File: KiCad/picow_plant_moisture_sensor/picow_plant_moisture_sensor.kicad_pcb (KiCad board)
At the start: 4 copper layers, 74 x 52 mm, 52 parts, among them J2 AudioJack3, J3 Micro_SD_Card, J4 L77HDE15SD1CH4F, J7 Conn_02x03_Odd_Even, SW1 SW_Push, SW2 SW_Push, SW3 SW_Push, SW4 SW_Push, U1 TLV70033_SOT23-5, U2 PicoW, U3 NC7WZ16P6X

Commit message: First version done
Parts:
- removed C1, C2: 1u, Capacitor_SMD:C_0603_1608Metric
- removed C14, C15: 47u, Capacitor_SMD:C_0805_2012Metric
- removed C19: 10u, Capacitor_SMD:C_0603_1608Metric
- removed C4, C7, C8: 100n, Capacitor_SMD:C_0402_1005Metric
- removed R1, R2: 220, Resistor_SMD:R_0402_1005Metric
- removed R10, R11: 47, Resistor_SMD:R_0402_1005Metric
- removed R23, R24: 10k, Resistor_SMD:R_0402_1005Metric
- removed R26, R31, R36: 499, Resistor_SMD:R_0402_1005Metric
- removed R27, R32, R37: 1k, Resistor_SMD:R_0402_1005Metric
- removed R28, R33, R38: 2k, Resistor_SMD:R_0402_1005Metric
- removed R29, R34, R39: 4.02k, Resistor_SMD:R_0402_1005Metric
- removed R3, R4: 100, Resistor_SMD:R_0402_1005Metric
- removed R30, R35, R40: 8.06k, Resistor_SMD:R_0402_1005Metric
- removed R7, R8: 1.8K, Resistor_SMD:R_0402_1005Metric
- removed R9: DNF, Resistor_SMD:R_0402_1005Metric
- removed U1: TLV70033_SOT23-5, Package_TO_SOT_SMD:SOT-23-5
- removed U3: NC7WZ16P6X, Package_TO_SOT_SMD:SOT-363_SC-70-6
- added J1: Conn_01x03, Connector_PinHeader_2.54mm:PinHeader_1x03_P2.54mm_Horizontal, F.Cu at (106.4, 60.4)
- added J10: Conn_01x03, Connector_PinHeader_2.54mm:PinHeader_1x03_P2.54mm_Horizontal, F.Cu at (162.3, 65.5)
- added J11: Conn_01x03, Connector_PinHeader_2.54mm:PinHeader_1x03_P2.54mm_Horizontal, F.Cu at (162.3, 62.9)
- added J12: Conn_01x03, Connector_PinHeader_2.54mm:PinHeader_1x03_P2.54mm_Horizontal, F.Cu at (162.3, 60.4)
- added J13: Conn_01x03, Connector_PinHeader_2.54mm:PinHeader_1x03_P2.54mm_Horizontal, F.Cu at (162.3, 57.9)
- added J14: ADS1115, Connector_PinHeader_2.54mm:PinHeader_1x10_P2.54mm_Horizontal, F.Cu at (159.8, 57.9)
- added J15: ADS1115, Connector_PinHeader_2.54mm:PinHeader_1x10_P2.54mm_Horizontal, F.Cu at (103.9, 52.8)
- added J16: ADS1115, Connector_PinHeader_2.54mm:PinHeader_1x10_P2.54mm_Horizontal, F.Cu at (103.9, 78.2)
- added J5: Conn_01x03, Connector_PinHeader_2.54mm:PinHeader_1x03_P2.54mm_Horizontal, F.Cu at (106.4, 85.8)
- added J6: Conn_01x03, Connector_PinHeader_2.54mm:PinHeader_1x03_P2.54mm_Horizontal, F.Cu at (106.4, 83.3)
- added J8: Conn_01x03, Connector_PinHeader_2.54mm:PinHeader_1x03_P2.54mm_Horizontal, F.Cu at (106.4, 80.7)
- added J9: Conn_01x03, Connector_PinHeader_2.54mm:PinHeader_1x03_P2.54mm_Horizontal, F.Cu at (106.4, 78.2)
- J2: value AudioJack3 -> Conn_01x03; footprint RPi_Pico:CUI_SJ-3523-audio-jack -> Connector_PinHeader_2.54mm:PinHeader_1x03_P2.54mm_Horizontal
- J3: value Micro_SD_Card -> Conn_01x03; footprint Connector_Card:microSD_HC_Molex_104031-0811 -> Connector_PinHeader_2.54mm:PinHeader_1x03_P2.54mm_Horizontal
- J4: value L77HDE15SD1CH4F -> Conn_01x03; footprint RPi_Pico:DSUB-15-L77HDE15SD1CH4F -> Connector_PinHeader_2.54mm:PinHeader_1x03_P2.54mm_Horizontal
- moved J3 59.7 mm to (106.4, 55.3), turned to 90 degrees
- moved J2 55.1 mm to (106.4, 57.9), turned to 90 degrees
- moved J4 22.9 mm to (106.4, 52.8)
- moved SW4 22.4 mm to (111.0, 69.1)
- moved SW1 16.3 mm to (159.3, 89.4)
- moved SW2 16.0 mm to (111.0, 99.6)
- moved SW3 7.14 mm to (111.0, 92.0)
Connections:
- J2 pad 1: GND -> /AIN5
- J2 pad 2: /PWM_AUDIO_L -> +3V3
- J2 pad 3: /PWM_AUDIO_R -> GND
- J3 pad 1: /SD_DAT2 -> /AIN6
- J3 pad 2: /GPIO22 -> +3V3
- J3 pad 3: /GPIO18 -> GND
- J4 pad 1: /VGA_R -> /AIN7
- J4 pad 2: /VGA_G -> +3V3
- J4 pad 3: /VGA_B -> GND
- J7 pad 2: /SD_DAT2 -> /GPIO21
- J7 pad 4: /SD_DAT1 -> /GPIO20
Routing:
- net /HSYNC: track 89.2 -> 0.00 mm, vias 1 -> 0
- net /GPIO8: track 5.37 -> 91.0 mm
- net /GPIO9: track 5.37 -> 82.6 mm
- net /VSYNC: track 73.1 -> 0.00 mm, vias 1 -> 0
- net /GPIO5: track 56.4 -> 0.00 mm, vias 2 -> 0
- net +3V3: track 123.4 -> 173.4 mm, vias 4 -> 1
- net /GPIO18: track 35.4 -> 0.00 mm, vias 2 -> 0
- net /VGA_B: track 30.9 -> 0.00 mm, vias 1 -> 0
- net /GPIO19: track 29.9 -> 0.00 mm
- net /GPIO22: track 29.7 -> 0.00 mm, vias 2 -> 0
- net /VGA_G: track 28.5 -> 0.00 mm
- net /SD_DAT2: track 27.4 -> 0.00 mm
- net /VGA_R: track 25.9 -> 0.00 mm
- net GND: track 25.0 -> 0.00 mm, vias 60 -> 0
- net /SD_DAT1: track 20.3 -> 0.00 mm
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- removed copper zone on In1.Cu, net GND
- removed copper zone on In2.Cu, net GND
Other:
- board size 74 x 52 mm -> 78.7 x 55.9 mm
- copper layers 4 -> 2

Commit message: V1 done
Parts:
- J1, J10, J11, J12, J13, J2, J3, J4, J5, J6, J8, J9: footprint Connector_PinHeader_2.54mm:PinHeader_1x03_P2.54mm_Horizontal -> Connector_PinHeader_2.54mm:PinHeader_1x03_P2.54mm_Vertical
- J14, J15, J16: footprint Connector_PinHeader_2.54mm:PinHeader_1x10_P2.54mm_Horizontal -> Connector_PinHeader_2.54mm:PinHeader_1x10_P2.54mm_Vertical

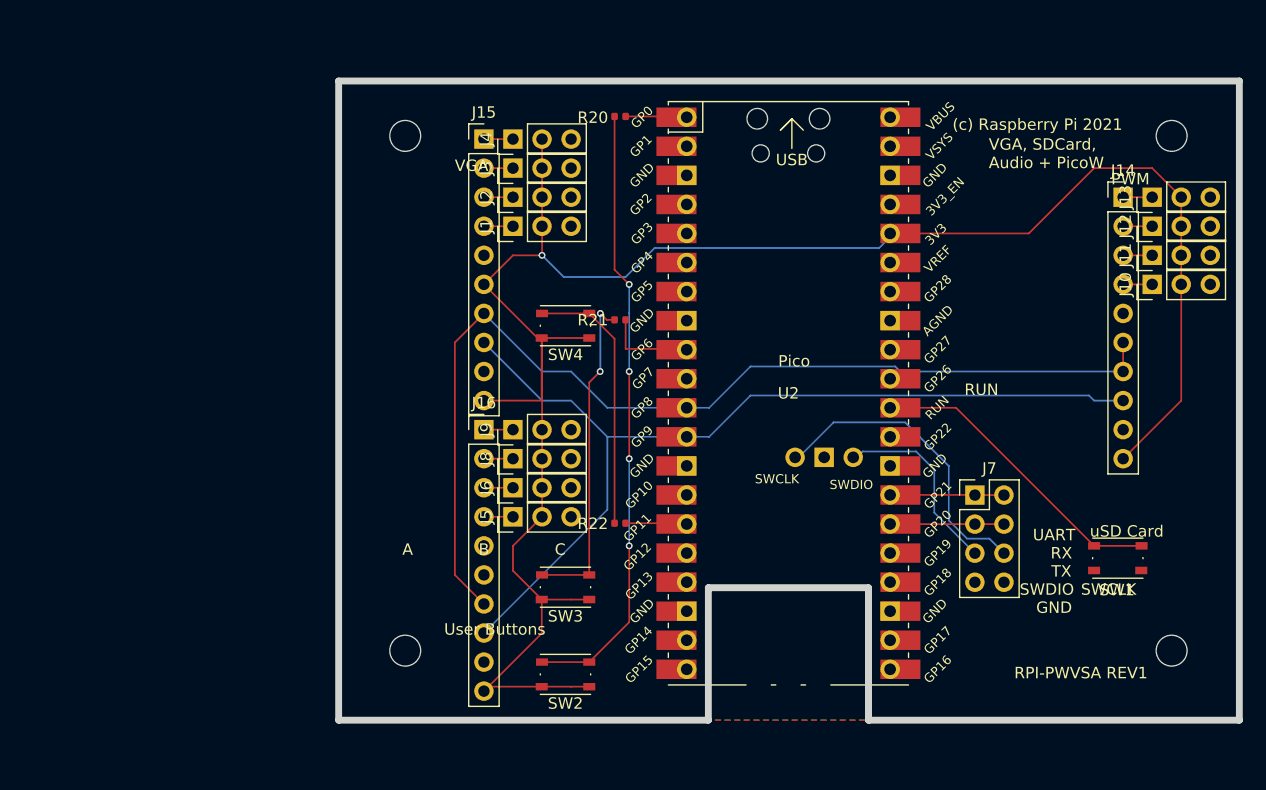
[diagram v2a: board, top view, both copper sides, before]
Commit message: 10 pcb design with ics instead of complete pcb on headers (#11)
* No traces

* Routing done

* Complete PCB design with component references

* Rev1 ordered
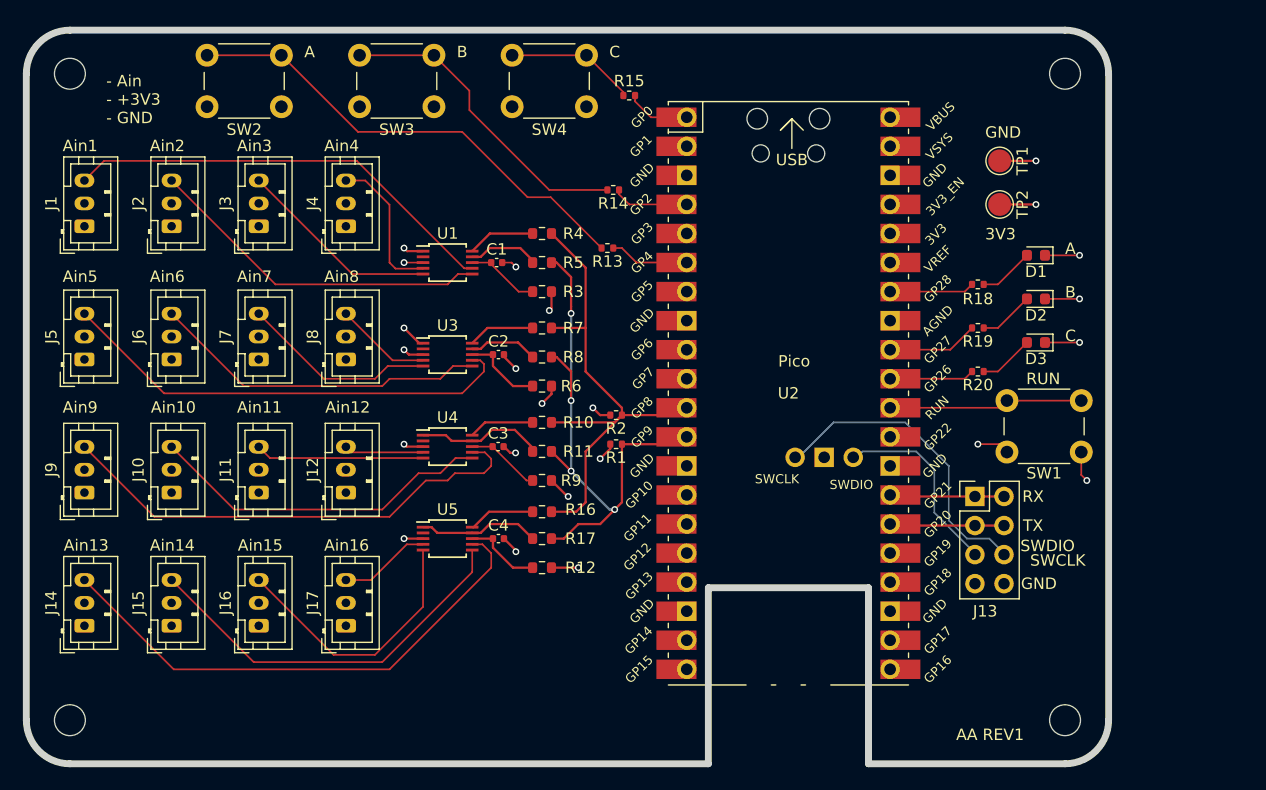
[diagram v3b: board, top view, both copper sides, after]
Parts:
- removed R21, R22: 1k, Resistor_SMD:R_0402_1005Metric
- added C1: 100n, Capacitor_SMD:C_0402_1005Metric, F.Cu at (105.0, 63.6)
- added C2: 100n, Capacitor_SMD:C_0402_1005Metric, F.Cu at (105.2, 71.6)
- added C3: 100n, Capacitor_SMD:C_0402_1005Metric, F.Cu at (105.1, 79.7)
- added C4: 100n, Capacitor_SMD:C_0402_1005Metric, F.Cu at (105.2, 87.7)
- added D1: LED, LED_SMD:LED_0603_1608Metric, F.Cu at (152.1, 62.9)
- added D2: LED, LED_SMD:LED_0603_1608Metric, F.Cu at (152.1, 66.8)
- added D3: LED, LED_SMD:LED_0603_1608Metric, F.Cu at (152.1, 70.6)
- added J17: Conn_01x03, Connector_JST:JST_PH_B3B-PH-K_1x03_P2.00mm_Vertical, F.Cu at (91.8, 95.3)
- added R1: 5k, Resistor_SMD:R_0402_1005Metric, F.Cu at (115.4, 79.5)
- added R10: 0, Resistor_SMD:R_0603_1608Metric, F.Cu at (109.0, 77.5)
- added R11: 0, Resistor_SMD:R_0603_1608Metric, F.Cu at (109.0, 80.1)
- added R12: 0, Resistor_SMD:R_0603_1608Metric, F.Cu at (109.0, 90.2)
- added R13: 1k, Resistor_SMD:R_0402_1005Metric, F.Cu at (114.7, 62.3)
- added R14: 1k, Resistor_SMD:R_0402_1005Metric, F.Cu at (115.2, 57.2)
- added R15: 1k, Resistor_SMD:R_0402_1005Metric, F.Cu at (116.6, 49.0)
- added R16: 0, Resistor_SMD:R_0603_1608Metric, F.Cu at (109.0, 85.4)
- added R17: 0, Resistor_SMD:R_0603_1608Metric, F.Cu at (109.0, 87.7)
- added R18: 330, Resistor_SMD:R_0402_1005Metric, F.Cu at (147.1, 65.5)
- added R19: 330, Resistor_SMD:R_0402_1005Metric, F.Cu at (147.1, 69.3)
- added R2: 5k, Resistor_SMD:R_0402_1005Metric, F.Cu at (115.4, 76.9)
- added R3: 0, Resistor_SMD:R_0603_1608Metric, F.Cu at (109.0, 66.1)
- added R4: 0, Resistor_SMD:R_0603_1608Metric, F.Cu at (109.0, 61.0)
- added R5: 0, Resistor_SMD:R_0603_1608Metric, F.Cu at (109.0, 63.6)
- added R6: 0, Resistor_SMD:R_0603_1608Metric, F.Cu at (109.0, 74.4)
- added R7: 0, Resistor_SMD:R_0603_1608Metric, F.Cu at (109.0, 69.3)
- added R8: 0, Resistor_SMD:R_0603_1608Metric, F.Cu at (109.0, 71.8)
- added R9: 0, Resistor_SMD:R_0603_1608Metric, F.Cu at (109.0, 82.6)
- added TP1: TestPoint, TestPoint:TestPoint_Pad_D2.0mm, F.Cu at (149.0, 54.7)
- added TP2: TestPoint, TestPoint:TestPoint_Pad_D2.0mm, F.Cu at (149.0, 58.5)
- added U1: ADS1115IDGS, Package_SO:TSSOP-10_3x3mm_P0.5mm, F.Cu at (100.7, 63.6)
- added U3: ADS1115IDGS, Package_SO:TSSOP-10_3x3mm_P0.5mm, F.Cu at (100.7, 71.6)
- added U4: ADS1115IDGS, Package_SO:TSSOP-10_3x3mm_P0.5mm, F.Cu at (100.7, 79.7)
- added U5: ADS1115IDGS, Package_SO:TSSOP-10_3x3mm_P0.5mm, F.Cu at (100.7, 87.7)
- J1, J10, J11, J12, J2, J3, J4, J5, J6, J8, J9: footprint Connector_PinHeader_2.54mm:PinHeader_1x03_P2.54mm_Vertical -> Connector_JST:JST_PH_B3B-PH-K_1x03_P2.00mm_Vertical
- J13: value Conn_01x03 -> Conn_02x03_Odd_Even; footprint Connector_PinHeader_2.54mm:PinHeader_1x03_P2.54mm_Vertical -> Connector_PinHeader_2.54mm:PinHeader_2x04_P2.54mm_Vertical
- J14, J15, J16: value ADS1115 -> Conn_01x03; footprint Connector_PinHeader_2.54mm:PinHeader_1x10_P2.54mm_Vertical -> Connector_JST:JST_PH_B3B-PH-K_1x03_P2.00mm_Vertical
- J7: value Conn_02x03_Odd_Even -> Conn_01x03; footprint Connector_PinHeader_2.54mm:PinHeader_2x04_P2.54mm_Vertical -> Connector_JST:JST_PH_B3B-PH-K_1x03_P2.00mm_Vertical
- R20: value 1k -> 330
- SW1, SW2, SW3, SW4: footprint Button_Switch_SMD:SW_Push_1P1T_NO_Vertical_Wuerth_434133025816 -> Button_Switch_THT:SW_PUSH_6mm
- moved J14 98.2 mm to (69.0, 95.3), turned to 90 degrees
- moved J10 87.6 mm to (76.6, 83.7)
- moved J11 80.8 mm to (84.2, 83.7)
- moved J12 74.2 mm to (91.8, 83.7)
- moved J7 63.7 mm to (84.2, 72.0), turned to 90 degrees
- moved SW2 55.5 mm to (86.2, 50.0)
- moved J15 50.6 mm to (76.6, 95.3), turned to 90 degrees
- moved SW3 43.6 mm to (99.5, 50.0)
- moved J5 39.9 mm to (69.0, 72.0)
- moved R20 38.4 mm to (147.1, 73.1)
- moved J9 37.9 mm to (69.0, 83.7)
- moved J1 37.5 mm to (69.0, 60.4)
- moved J6 31.9 mm to (76.6, 72.0)
- moved J13 30.4 mm to (146.8, 84.0), turned to 0 degrees
- moved J2 30.0 mm to (76.6, 60.4)
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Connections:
- J1 pad 1: /AIN4 -> GND
- J1 pad 3: GND -> /AIN0
- J10 pad 1: /AIN8 -> GND
- J10 pad 3: GND -> /AIN9
- J11 pad 1: /AIN9 -> GND
- J11 pad 3: GND -> /AIN10
- J12 pad 1: /AIN10 -> GND
- J12 pad 3: GND -> /AIN11
- J13 pad 1: /AIN11 -> /GPIO21
- J13 pad 2: +3V3 -> /GPIO21
- J13 pad 3: GND -> /GPIO20
- J14 pad 1: /AIN11 -> GND
- J14 pad 2: /AIN10 -> +3V3
- J14 pad 3: /AIN9 -> /AIN12
- J15 pad 1: /AIN7 -> GND
- J15 pad 2: /AIN6 -> +3V3
- J15 pad 3: /AIN5 -> /AIN13
- J16 pad 1: /AIN3 -> GND
- J16 pad 2: /AIN2 -> +3V3
- J16 pad 3: /AIN1 -> /AIN14
- J2 pad 1: /AIN5 -> GND
- J2 pad 3: GND -> /AIN1
- J3 pad 1: /AIN6 -> GND
- J3 pad 3: GND -> /AIN2
- J4 pad 1: /AIN7 -> GND
- J4 pad 3: GND -> /AIN3
- J5 pad 1: /AIN0 -> GND
- J5 pad 3: GND -> /AIN4
- J6 pad 1: /AIN1 -> GND
- J6 pad 3: GND -> /AIN5
- J7 pad 1: /GPIO21 -> GND
- J7 pad 2: /GPIO21 -> +3V3
- J7 pad 3: /GPIO20 -> /AIN6
- J8 pad 1: /AIN2 -> GND
- J8 pad 3: GND -> /AIN7
- J9 pad 1: /AIN3 -> GND
- J9 pad 3: GND -> /AIN8
- R20 pad 1: /GPIO0 -> Net-(D3-A)
- R20 pad 2: Net-(R20-Pad2) -> /GPIO26
- SW2 pad 2: Net-(R20-Pad2) -> Net-(R13-Pad2)
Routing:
- net +3V3: track 173.4 -> 16.8 mm, vias 1 -> 8
- net Net-(R20-Pad2): track 53.8 -> 0.00 mm, vias 4 -> 0
- net /AIN12: track 0.00 -> 45.7 mm
- net /GPIO8: track 91.0 -> 46.0 mm
- net Net-(R13-Pad2): track 0.00 -> 41.5 mm
- net /AIN8: track 2.54 -> 42.5 mm
- net /AIN4: track 2.54 -> 40.4 mm
- net /AIN0: track 2.54 -> 38.5 mm
- net /AIN13: track 0.00 -> 34.4 mm
- net /GPIO9: track 82.6 -> 50.1 mm, vias 0 -> 4
- net GND: track 0.00 -> 32.3 mm, vias 0 -> 15
- net /AIN9: track 2.54 -> 30.4 mm
- net /AIN1: track 2.54 -> 30.4 mm
- net /AIN5: track 2.54 -> 29.6 mm
- net /AIN14: track 0.00 -> 23.8 mm
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- added copper zone on In2.Cu, net +3V3
- added copper zone on In1.Cu, net GND
- removed copper zone on B.Cu, net GND
- removed copper zone on F.Cu, net GND
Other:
- board size 78.7 x 55.9 mm -> 94.6 x 64.1 mm
- copper layers 2 -> 4
- board text added: "- Ain - +3V3 - GND"
- board text added: "3V3"
- board text added: "AA REV1"
- board text added: "Ain1"
- board text added: "Ain10"
- board text added: "Ain11"
- board text added: "Ain12"
- board text added: "Ain13"
- board text added: "Ain14"
- board text added: "Ain15"
- board text added: "Ain16"
- board text added: "Ain2"
- board text added: "Ain3"
- board text added: "Ain4"
- board text added: "Ain5"
- board text added: "Ain6"
- board text added: "Ain7"
- board text added: "Ain8"
- board text added: "Ain9"
- board text removed: "(c) Raspberry Pi 2021"
- board text removed: "PWM"
- board text removed: "RPI-PWVSA REV1"
- board text removed: "UART"
- board text removed: "User Buttons"
- board text removed: "VGA"
- board text removed: "VGA, SDCard, Audio + PicoW"
- board text removed: "uSD Card"

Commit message: Add rev2 (#33)
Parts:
- added R21: 5k, Resistor_SMD:R_0603_1608Metric, F.Cu at (144.5, 78.8)
- added R22: 5k, Resistor_SMD:R_0603_1608Metric, F.Cu at (144.5, 81.3)
- added TP3: TestPoint, TestPoint:TestPoint_Pad_D2.0mm, F.Cu at (97.5, 56.0)
- added TP4: TestPoint, TestPoint:TestPoint_Pad_D2.0mm, F.Cu at (101.3, 57.2)
- added U6: 24LC16, 24LC16B-I_SN:SOIC127P600X175-8N, F.Cu at (149.7, 99.1)
- C1, C2, C3, C4: footprint Capacitor_SMD:C_0402_1005Metric -> Capacitor_SMD:C_0603_1608Metric
- R1, R13, R14, R15, R18, R19, R2, R20: footprint Resistor_SMD:R_0402_1005Metric -> Resistor_SMD:R_0603_1608Metric
- moved R14 1.14 mm to (114.0, 57.2)
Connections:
- J13 pad 1: /GPIO21 -> /GPIO17
- J13 pad 2: /GPIO21 -> /SWCLK
- J13 pad 3: /GPIO20 -> /GPIO16
- J13 pad 4: /GPIO20 -> GND
- J13 pad 5: /SWDIO -> GND
- J13 pad 6: /SWCLK -> /SWDIO
- R10 pad 2: /GPIO8 -> /GPIO9
- R11 pad 2: /GPIO9 -> /GPIO8
- R16 pad 2: /GPIO8 -> /GPIO9
- R17 pad 2: /GPIO9 -> /GPIO8
- R4 pad 2: /GPIO8 -> /GPIO9
- R5 pad 2: /GPIO9 -> /GPIO8
- R7 pad 2: /GPIO8 -> /GPIO9
- R8 pad 2: /GPIO9 -> /GPIO8
- U1 pad 4: /AIN3 -> /AIN0
- U1 pad 5: /AIN2 -> /AIN1
- U1 pad 6: /AIN1 -> /AIN2
- U1 pad 7: /AIN0 -> /AIN3
- U3 pad 4: /AIN7 -> /AIN4
- U3 pad 5: /AIN6 -> /AIN5
- U3 pad 6: /AIN5 -> /AIN6
- U3 pad 7: /AIN4 -> /AIN7
- U4 pad 4: /AIN11 -> /AIN8
- U4 pad 5: /AIN10 -> /AIN9
- U4 pad 6: /AIN9 -> /AIN10
- U4 pad 7: /AIN8 -> /AIN11
- U5 pad 4: /AIN15 -> /AIN12
- U5 pad 5: /AIN14 -> /AIN13
- U5 pad 6: /AIN13 -> /AIN14
- U5 pad 7: /AIN12 -> /AIN15
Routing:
- net /GPIO21: track 10.0 -> 41.9 mm
- net /GPIO20: track 10.0 -> 38.5 mm
- net /GPIO8: track 46.0 -> 64.6 mm, vias 0 -> 2
- net /GPIO17: track 0.00 -> 17.5 mm
- net /GPIO16: track 0.00 -> 16.5 mm
- net /AIN12: track 45.7 -> 30.9 mm
- net /AIN13: track 34.4 -> 23.1 mm
- net /AIN8: track 42.5 -> 33.3 mm
- net /AIN10: track 14.8 -> 22.8 mm
- net /AIN9: track 30.4 -> 24.2 mm
- net /GPIO9: track 50.1 -> 55.8 mm
- net +3V3: track 16.8 -> 22.4 mm, vias 8 -> 11
- net GND: track 32.3 -> 37.7 mm, vias 15 -> 17
- net /AIN4: track 40.4 -> 35.1 mm, vias 0 -> 1
- net /AIN1: track 30.4 -> 25.4 mm
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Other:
- outline, holes or cut-outs redrawn
- board text added: "AA REV2"
- board text added: "SCL"
- board text added: "SDA"
- board text removed: "AA REV1"
